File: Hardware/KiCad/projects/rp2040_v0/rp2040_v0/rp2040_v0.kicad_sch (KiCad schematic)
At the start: 59 parts, among them J1 Conn_01x03, J10 Screw_Terminal_01x02, J11 Conn_01x02, J12 Screw_Terminal_01x02, J2 Conn_01x02, J3 Conn_01x03, J4 Conn_01x04, J5 USB_B_Micro, J6 Conn_01x02, J7 Conn_01x02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

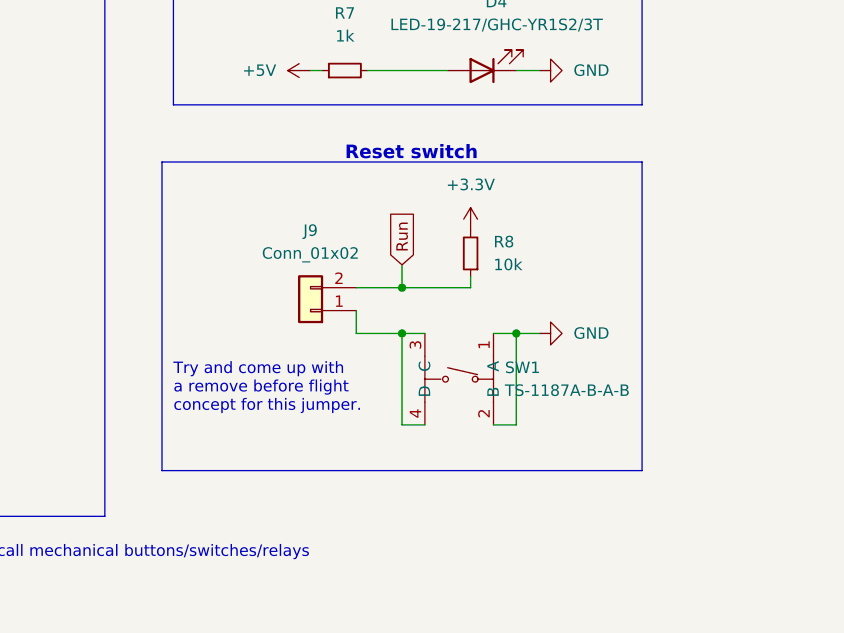
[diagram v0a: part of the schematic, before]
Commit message: PCB is WAY too big. Start optimizing and update to v0.1.
Removes reset push button
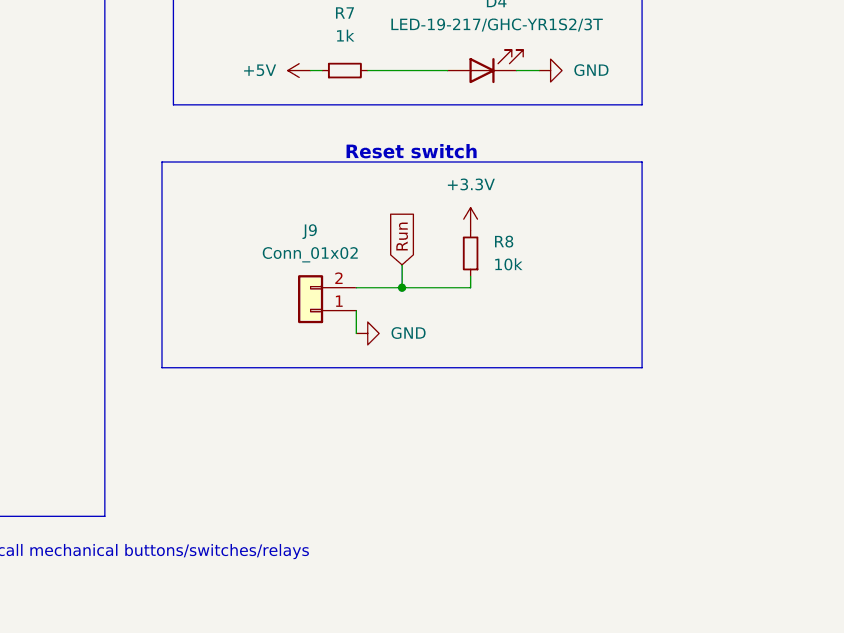
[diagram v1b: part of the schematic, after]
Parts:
- removed SW1: TS-1187A-B-A-B, easyeda2kicad:SW-SMD_4P-L5.1-W5.1-P3.70-LS6.5-TL-2, symbol easyeda2kicad:TS-1187A-B-A-B
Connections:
- net -BATT: now also J9.1 (Pin_1)
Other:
- note removed: "Try and come up with a remove before flight concept for this jumper."
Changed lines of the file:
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@@
   (title_block
     (title "rp2040 Flight Computer")
-    (date "2023-01-28")
-    (rev "v0")
+    (date "2023-01-29")
+    (rev "v0.1")
   )
   (junction (at 134.62 187.96) (diameter 0) (color 0 0 0 0)
@@
   (junction (at 205.74 71.12) (diameter 0) (color 0 0 0 0)
   )
-  (junction (at 257.81 144.78) (diameter 0) (color 0 0 0 0)
-  )
-  (junction (at 270.51 144.78) (diameter 0) (color 0 0 0 0)
-  )
   (junction (at 62.23 33.02) (diameter 0) (color 0 0 0 0)
   )
@@
     (stroke (width 0) (type default) (color 0 0 0 0))
   )
-  (wire (pts (xy 267.97 144.78) (xy 270.51 144.78))
-    (stroke (width 0) (type default) (color 0 0 0 0))
-  )
   (wire (pts (xy 62.23 167.64) (xy 62.23 165.1))
     (stroke (width 0) (type default) (color 0 0 0 0))
@@
     (stroke (width 0) (type default) (color 0 0 0 0))
   )
-  (wire (pts (xy 270.51 154.94) (xy 270.51 144.78))
-    (stroke (width 0) (type default) (color 0 0 0 0))
-  )
   (wire (pts (xy 160.02 71.12) (xy 170.18 71.12))
     (stroke (width 0) (type default) (color 0 0 0 0))
@@
     (stroke (width 0) (type default) (color 0 0 0 0))
   )
-  (wire (pts (xy 257.81 144.78) (xy 260.35 144.78))
-    (stroke (width 0) (type default) (color 0 0 0 0))
-  )
   (polyline (pts (xy 232.41 81.28) (xy 284.48 81.28))
     (stroke (width 0) (type default) (color 0 0 0 0))
@@
     (stroke (width 0) (type default) (color 0 0 0 0))
   )
-  (polyline (pts (xy 231.14 125.73) (xy 231.14 160.02))
+  (polyline (pts (xy 231.14 125.73) (xy 231.14 148.59))
     (stroke (width 0) (type default) (color 0 0 0 0))
   )
@@
     (stroke (width 0) (type default) (color 0 0 0 0))
   )
-  (wire (pts (xy 270.51 144.78) (xy 273.05 144.78))
-    (stroke (width 0) (type default) (color 0 0 0 0))
-  )
   (wire (pts (xy 257.81 72.39) (xy 261.62 72.39))
     (stroke (width 0) (type default) (color 0 0 0 0))
@@
     (stroke (width 0) (type default) (color 0 0 0 0))
   )
-  (wire (pts (xy 252.73 144.78) (xy 257.81 144.78))
-    (stroke (width 0) (type default) (color 0 0 0 0))
-  )
   (wire (pts (xy 214.63 71.12) (xy 214.63 73.66))
     (stroke (width 0) (type default) (color 0 0 0 0))
@@
     (stroke (width 0) (type default) (color 0 0 0 0))
   )
-  (wire (pts (xy 260.35 154.94) (xy 257.81 154.94))
-    (stroke (width 0) (type default) (color 0 0 0 0))
-  )
   (wire (pts (xy 67.31 101.6) (xy 67.31 104.14))
     (stroke (width 0) (type default) (color 0 0 0 0))
@@
     (stroke (width 0) (type default) (color 0 0 0 0))
   )
-  (polyline (pts (xy 284.48 125.73) (xy 284.48 160.02))
+  (polyline (pts (xy 284.48 125.73) (xy 284.48 148.59))
     (stroke (width 0) (type default) (color 0 0 0 0))
   )
@@
     (stroke (width 0) (type default) (color 0 0 0 0))
   )
-  (wire (pts (xy 257.81 154.94) (xy 257.81 144.78))
-    (stroke (width 0) (type default) (color 0 0 0 0))
-  )
   (wire (pts (xy 144.78 34.29) (xy 144.78 35.56))
     (stroke (width 0) (type default) (color 0 0 0 0))
@@
     (stroke (width 0) (type default) (color 0 0 0 0))
   )
-  (polyline (pts (xy 231.14 160.02) (xy 284.48 160.02))
+  (polyline (pts (xy 231.14 148.59) (xy 284.48 148.59))
     (stroke (width 0) (type default) (color 0 0 0 0))
   )
@@
     (stroke (width 0) (type default) (color 0 0 0 0))
   )
-  (wire (pts (xy 267.97 154.94) (xy 270.51 154.94))
-    (stroke (width 0) (type default) (color 0 0 0 0))
-  )
   (wire (pts (xy 116.84 93.98) (xy 118.11 93.98))
     (stroke (width 0) (type default) (color 0 0 0 0))
@@
     (effects (font (size 1.27 1.27)) (justify left bottom))
   )
-  (text "Try and come up with\na remove before flight\nconcept for this jumper."
-    (at 232.41 153.67 0)
-    (effects (font (size 1.27 1.27)) (justify left bottom))
-  )
   (text "Termination resistors\nneed to be placed\nclose to chip."
     (at 90.17 102.87 0)
@@
     (pin "2")
   )
-  (symbol (lib_id "easyeda2kicad:TS-1187A-B-A-B") (at 265.43 149.86 270) (unit 1)
-    (in_bom yes) (on_board yes) (fields_autoplaced)
-    (property "Reference" "SW1" (id 0) (at 269.24 148.5899 90)
-      (effects (font (size 1.27 1.27)) (justify left))
-    )
-    (property "Value" "TS-1187A-B-A-B" (id 1) (at 269.24 151.1299 90)
-      (effects (font (size 1.27 1.27)) (justify left))
-    )
-    (property "Footprint" "easyeda2kicad:SW-SMD_4P-L5.1-W5.1-P3.70-LS6.5-TL-2" (id 2) (at 252.73 149.86 0)
-      (effects (font (size 1.27 1.27)) hide)
-    )
-    (property "Datasheet" "https://lcsc.com/product-detail/Tactile-Switches_XKB-Enterprise-TS-1187-B-A-A_C318884.html" (id 3) (at 250.19 149.86 0)
-      (effects (font (size 1.27 1.27)) hide)
-    )
-    (property "Manufacturer" "XKB Connectivity(中国星坤)" (id 4) (at 247.65 149.86 0)
-      (effects (font (size 1.27 1.27)) hide)
-    )
-    (property "LCSC Part" "C318884" (id 5) (at 245.11 149.86 0)
-      (effects (font (size 1.27 1.27)) hide)
-    )
-    (property "JLC Part" "Basic Part" (id 6) (at 242.57 149.86 0)
-      (effects (font (size 1.27 1.27)) hide)
-    )
-    (pin "1")
-    (pin "2")
-    (pin "3")
-    (pin "4")
-  )
   (symbol (lib_id "power:+3.3V") (at 247.65 99.06 90) (unit 1)
     (in_bom yes) (on_board yes) (fields_autoplaced)
@@
     (pin "1")
   )
-  (symbol (lib_id "power:GND") (at 273.05 144.78 90) (unit 1)
+  (symbol (lib_id "power:GND") (at 252.73 144.78 90) (unit 1)
     (in_bom yes) (on_board yes) (fields_autoplaced)
-    (property "Reference" "#PWR032" (id 0) (at 279.4 144.78 0)
+    (property "Reference" "#PWR032" (id 0) (at 259.08 144.78 0)
       (effects (font (size 1.27 1.27)) hide)
     )
-    (property "Value" "GND" (id 1) (at 276.86 144.7799 90)
+    (property "Value" "GND" (id 1) (at 256.54 144.7799 90)
       (effects (font (size 1.27 1.27)) (justify right))
     )
-    (property "Footprint" "" (id 2) (at 273.05 144.78 0)
+    (property "Footprint" "" (id 2) (at 252.73 144.78 0)
       (effects (font (size 1.27 1.27)) hide)
     )
-    (property "Datasheet" "" (id 3) (at 273.05 144.78 0)
+    (property "Datasheet" "" (id 3) (at 252.73 144.78 0)
       (effects (font (size 1.27 1.27)) hide)
     )
@@
       (reference "R59") (unit 1) (value "470") (footprint "Resistor_SMD:R_0402_1005Metric")
     )
-    (path "/7efa55e8-1139-47c5-8cd9-c816e910ebeb"
-      (reference "SW1") (unit 1) (value "TS-1187A-B-A-B") (footprint "easyeda2kicad:SW-SMD_4P-L5.1-W5.1-P3.70-LS6.5-TL-2")
-    )
     (path "/ca4db203-4ae9-4706-a083-67cd713f5b1d"

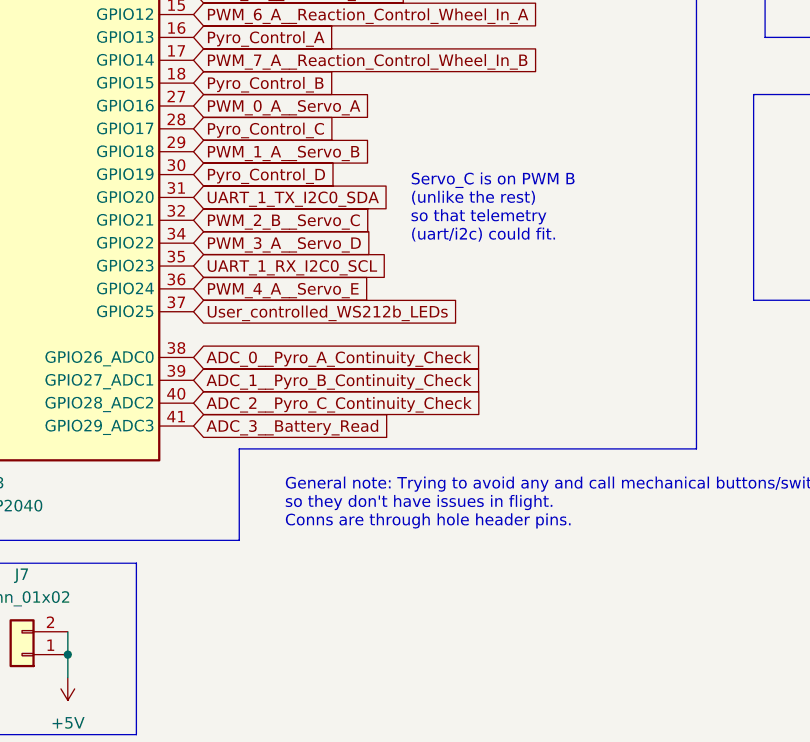
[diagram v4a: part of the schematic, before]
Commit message: Remove pyro channel D
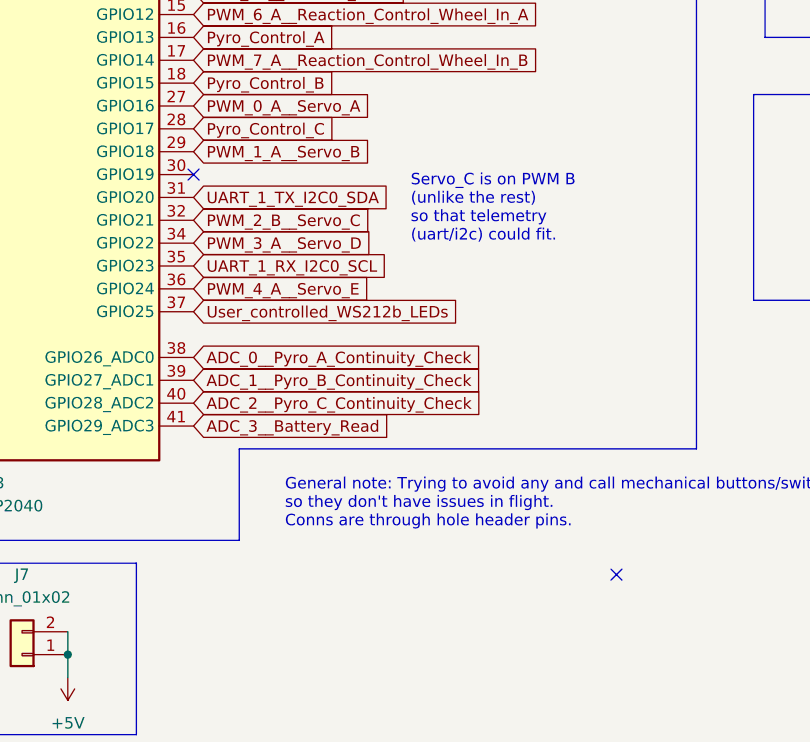
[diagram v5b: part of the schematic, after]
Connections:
- net Pyro_Control_D: no longer names the net of U3.30 (GPIO19)
- no-connect marks 1 -> 3
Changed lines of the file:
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@@
   (junction (at 140.97 64.77) (diameter 0) (color 0 0 0 0)
   )
+  (no_connect (at 215.9 179.07))
   (no_connect (at 132.08 46.99))
+  (no_connect (at 168.91 134.62))
   (polyline (pts (xy 284.48 49.53) (xy 254 49.53))
     (stroke (width 0) (type default) (color 0 0 0 0))
@@
     )
   )
-  (global_label "Pyro_Control_D" (shape input) (at 168.91 134.62 0) (fields_autoplaced)
-    (effects (font (size 1.27 1.27)) (justify left))
-    (property "Intersheet References" "${INTERSHEET_REFS}" (id 0) (at 177.6731 134.5406 0)
-      (effects (font (size 1.27 1.27)) (justify left) hide)
-    )
-  )
   (global_label "Protected_VBATT+" (shape input) (at 24.13 33.02 0) (fields_autoplaced)
     (effects (font (size 1.27 1.27)) (justify left))
@@
       (reference "#PWR080") (unit 1) (value "GND") (footprint "")
     )
-    (path "/5973b2d7-3984-4261-9bd9-41fa219882e0/1d686677-02fc-44f9-b645-70b541b1fac2"
-      (reference "#PWR081") (unit 1) (value "GND") (footprint "")
-    )
-    (path "/5973b2d7-3984-4261-9bd9-41fa219882e0/36e83c38-1a6e-4dea-b415-7a647b5d6647"
-      (reference "#PWR082") (unit 1) (value "GND") (footprint "")
-    )
     (path "/5973b2d7-3984-4261-9bd9-41fa219882e0/b09257f9-3560-430e-b02f-b37c889b3a74"
       (reference "#PWR083") (unit 1) (value "GND") (footprint "")
@@
       (reference "J25") (unit 1) (value "Screw_Terminal_01x02") (footprint "easyeda2kicad:CONN-TH_XY301V-A-5.0-2P")
     )
-    (path "/5973b2d7-3984-4261-9bd9-41fa219882e0/8e208824-1f96-40f3-8a2b-3647fddee4aa"
-      (reference "J26") (unit 1) (value "Screw_Terminal_01x02") (footprint "easyeda2kicad:CONN-TH_XY301V-A-5.0-2P")
-    )
     (path "/5973b2d7-3984-4261-9bd9-41fa219882e0/35b8318f-09e0-498c-a90e-e08a06ea135c"
       (reference "J27") (unit 1) (value "Screw_Terminal_01x02") (footprint "easyeda2kicad:CONN-TH_XY301V-A-5.0-2P")
@@
       (reference "Q2") (unit 1) (value "AO3400A") (footprint "Package_TO_SOT_SMD:SOT-23")
     )
-    (path "/5973b2d7-3984-4261-9bd9-41fa219882e0/baedc7a7-90c4-4f80-a592-1891b1c3560f"
-      (reference "Q3") (unit 1) (value "AO3400A") (footprint "Package_TO_SOT_SMD:SOT-23")
-    )
     (path "/5973b2d7-3984-4261-9bd9-41fa219882e0/7775d1c7-63e2-4a6f-9834-49916c0155ad"
       (reference "Q4") (unit 1) (value "AO3400A") (footprint "Package_TO_SOT_SMD:SOT-23")
@@
       (reference "R49") (unit 1) (value "DNP") (footprint "easyeda2kicad:RES-TH_BD2.4-L6.3-P10.30-D0.6")
     )
-    (path "/5973b2d7-3984-4261-9bd9-41fa219882e0/0d9e686c-bf8e-441d-be17-a3da5ed5785c"
-      (reference "R50") (unit 1) (value "10k") (footprint "Resistor_SMD:R_0402_1005Metric")
-    )
-    (path "/5973b2d7-3984-4261-9bd9-41fa219882e0/01a60961-78dd-4b7b-8815-2741d0edf649"
-      (reference "R51") (unit 1) (value "470") (footprint "Resistor_SMD:R_0402_1005Metric")
-    )
     (path "/5973b2d7-3984-4261-9bd9-41fa219882e0/613c5a50-26a1-48af-bd68-e51a30413dbe"

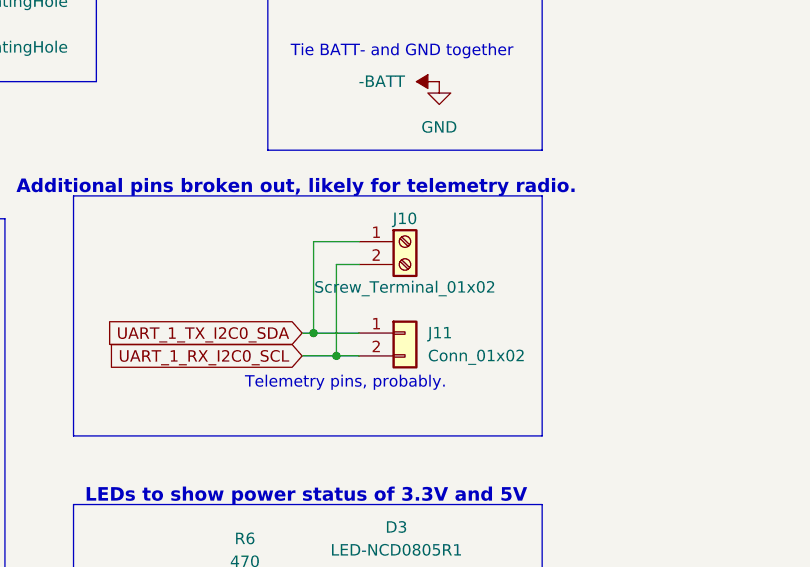
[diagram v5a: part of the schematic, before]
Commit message: Remove telelmetry screw terminal - leave header pin
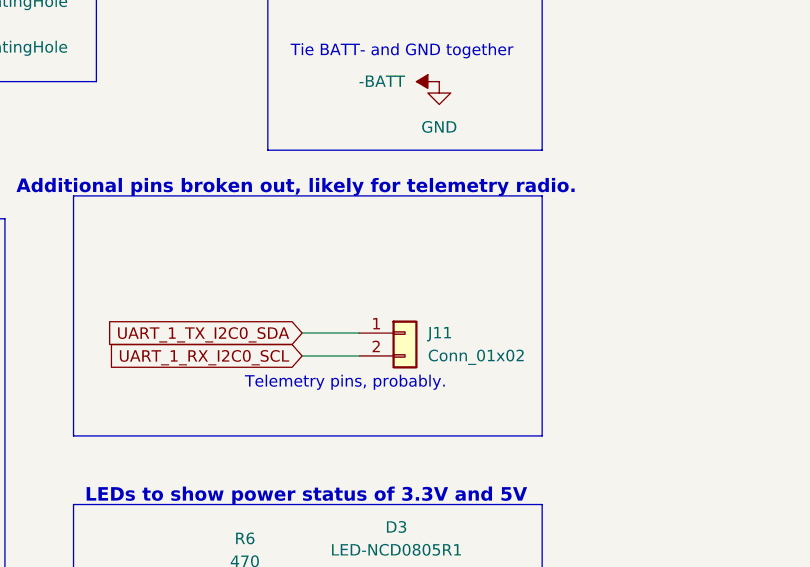
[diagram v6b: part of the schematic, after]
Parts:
- removed J10: Screw_Terminal_01x02, easyeda2kicad:CONN-TH_XY301V-A-5.0-2P, symbol Connector:Screw_Terminal_01x02
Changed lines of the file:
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@@
   (junction (at 40.64 93.98) (diameter 0) (color 0 0 0 0)
   )
-  (junction (at 259.08 69.85) (diameter 0) (color 0 0 0 0)
-  )
   (junction (at 130.81 64.77) (diameter 0) (color 0 0 0 0)
   )
@@
   (junction (at 187.96 66.04) (diameter 0) (color 0 0 0 0)
   )
-  (junction (at 261.62 72.39) (diameter 0) (color 0 0 0 0)
-  )
   (junction (at 160.02 66.04) (diameter 0) (color 0 0 0 0)
   )
@@
     (stroke (width 0) (type default) (color 0 0 0 0))
   )
-  (wire (pts (xy 261.62 62.23) (xy 264.16 62.23))
-    (stroke (width 0) (type default) (color 0 0 0 0))
-  )
   (polyline (pts (xy 12.7 17.78) (xy 102.87 17.78))
     (stroke (width 0) (type default) (color 0 0 0 0))
@@
     (stroke (width 0) (type default) (color 0 0 0 0))
   )
-  (wire (pts (xy 259.08 69.85) (xy 264.16 69.85))
+  (wire (pts (xy 257.81 69.85) (xy 264.16 69.85))
     (stroke (width 0) (type default) (color 0 0 0 0))
   )
@@
     (stroke (width 0) (type default) (color 0 0 0 0))
   )
-  (wire (pts (xy 259.08 69.85) (xy 259.08 59.69))
-    (stroke (width 0) (type default) (color 0 0 0 0))
-  )
-  (wire (pts (xy 261.62 72.39) (xy 264.16 72.39))
+  (wire (pts (xy 257.81 72.39) (xy 264.16 72.39))
     (stroke (width 0) (type default) (color 0 0 0 0))
   )
@@
     (stroke (width 0) (type default) (color 0 0 0 0))
   )
-  (wire (pts (xy 259.08 59.69) (xy 264.16 59.69))
-    (stroke (width 0) (type default) (color 0 0 0 0))
-  )
   (polyline (pts (xy 12.7 50.8) (xy 102.87 50.8))
     (stroke (width 0) (type default) (color 0 0 0 0))
   )
-  (wire (pts (xy 257.81 72.39) (xy 261.62 72.39))
-    (stroke (width 0) (type default) (color 0 0 0 0))
-  )
   (wire (pts (xy 153.67 73.66) (xy 153.67 74.93))
     (stroke (width 0) (type default) (color 0 0 0 0))
@@
     (stroke (width 0) (type default) (color 0 0 0 0))
   )
-  (wire (pts (xy 261.62 72.39) (xy 261.62 62.23))
-    (stroke (width 0) (type default) (color 0 0 0 0))
-  )
   (wire (pts (xy 134.62 187.96) (xy 134.62 190.5))
     (stroke (width 0) (type default) (color 0 0 0 0))
@@
     (stroke (width 0) (type default) (color 0 0 0 0))
   )
-  (wire (pts (xy 257.81 69.85) (xy 259.08 69.85))
-    (stroke (width 0) (type default) (color 0 0 0 0))
-  )
   (polyline (pts (xy 284.48 54.61) (xy 284.48 81.28))
     (stroke (width 0) (type default) (color 0 0 0 0))
@@
     (pin "3")
   )
-  (symbol (lib_id "Connector:Screw_Terminal_01x02") (at 269.24 59.69 0) (unit 1)
-    (in_bom yes) (on_board yes)
-    (property "Reference" "J10" (id 0) (at 269.24 57.15 0))
-    (property "Value" "Screw_Terminal_01x02" (id 1) (at 269.24 64.77 0))
-    (property "Footprint" "easyeda2kicad:CONN-TH_XY301V-A-5.0-2P" (id 2) (at 269.24 59.69 0)
-      (effects (font (size 1.27 1.27)) hide)
-    )
-    (property "Datasheet" "~" (id 3) (at 269.24 59.69 0)
-      (effects (font (size 1.27 1.27)) hide)
-    )
-    (pin "1")
-    (pin "2")
-  )
   (symbol (lib_id "power:+3.3V") (at 247.65 99.06 90) (unit 1)
     (in_bom yes) (on_board yes) (fields_autoplaced)
@@
       (reference "J9") (unit 1) (value "Conn_01x02") (footprint "Connector_PinHeader_2.54mm:PinHeader_1x02_P2.54mm_Vertical")
     )
-    (path "/7d9b36de-16cb-4948-81d2-5e0251d36e88"
-      (reference "J10") (unit 1) (value "Screw_Terminal_01x02") (footprint "easyeda2kicad:CONN-TH_XY301V-A-5.0-2P")
-    )
     (path "/bab6fd12-af94-4255-9b9f-edcfe4aeb46b"
